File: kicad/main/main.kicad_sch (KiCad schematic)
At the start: 16 parts

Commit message: Progress on circuit design
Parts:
- removed D2, D3, D4: SS14, PCM_JLCPCB:D_SMA, symbol PCM_JLCPCB-Diodes:Schottky,SS14
- removed L2, L3, L4: 68uH, EasyEDA_Lib:IND-SMD_L6.0-W6.0_FNR60XXS, symbol EasyEDA_Lib:FNR6045S680MT
- removed R2, R3, R4: 150mΩ, Resistor_SMD:R_1206_3216Metric_Pad1.30x1.75mm_HandSolder, symbol Device:R
- removed U2, U3, U4: (no value), EasyEDA_Lib:SOT-89-5_L4.5-W2.5-P1.50-LS4.5-BR, symbol EasyEDA_Lib:CL6807
- added C1, C2: 10uF, PCM_JLCPCB:C_0805, symbol PCM_JLCPCB-Capacitors:0805,10uF
- added C10, C13: 1uF, PCM_JLCPCB:C_0402, symbol PCM_JLCPCB-Capacitors:0402,1uF
- added C11, C12, C14, C3, C4, C5, C6, C7, C8: 100nF, PCM_JLCPCB:C_0402, symbol PCM_JLCPCB-Capacitors:0402,100nF
- added J1, J4, J5: Conn_01x02, Connector_Wire:SolderWire-0.75sqmm_1x02_P4.8mm_D1.25mm_OD2.3mm, symbol Connector_Generic:Conn_01x02
- added J2, J3: Conn_01x03, symbol Connector_Generic:Conn_01x03
- added J6: Connector, USB-TYPE-C-16P, PCM_JLCPCB:TYPE-C-SMD_HX-TYPE-C-16PIN, symbol PCM_JLCPCB-Extended:Connector, USB-TYPE-C-16P
- added R2, R3: 5.1kΩ, PCM_JLCPCB:R_0402, symbol PCM_JLCPCB-Resistors:0402,5.1kΩ
- added R4, R5: 27Ω, PCM_JLCPCB:R_0603, symbol PCM_JLCPCB-Resistors:0603,27Ω
- added R6: 1kΩ, PCM_JLCPCB:R_0402, symbol PCM_JLCPCB-Resistors:0402,1kΩ
- added S1, S2: Tactile Button, 160gf, PCM_JLCPCB:SW_TS-1088-AR02016, symbol PCM_JLCPCB-Connectors_Buttons:Tactile Button, 160gf, 12V, 50mA, 4.0mm
- added U2: XC6206P332MR, PCM_JLCPCB:SOT-23-3_L2.9-W1.6-P1.90-LS2.8-BR, symbol PCM_JLCPCB-Power:LDO, 3.3V, 0.2A
- added U3: (no value), EasyEDA_Lib:SOIC-8_L5.3-W5.3-P1.27-LS8.0-BL, symbol EasyEDA_Lib:W25Q16JVSSIQTR
- added U5: RP2040, PCM_JLCPCB:QFN-56-1EP_7x7mm_P0.4mm_EP3.2x3.2mm_ThermalVias, symbol PCM_JLCPCB-Extended:MCU, RP2040
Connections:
- net GND: now also C1.2, C10.2, C11.2, C12.2, C13.2, C14.1, C2.2, C3.2, C4.2, C5.2, C6.2, C7.2, C8.2, J2.3 (Pin_3), J3.3 (Pin_3), J6.A12B1 (GND), J6.B12A1 (GND), J6.S1 (SHIELD), R2.2, R3.1, S1.2 (B), S2.2 (B), U2.1 (GND), U3.4 (GND), U5.57 (GND)
- net +12V renamed +5V
- net +5V: now also C1.1, J2.1 (Pin_1), J3.1 (Pin_1), J4.1 (Pin_1), J5.1 (Pin_1), J6.A9B4 (VBUS), J6.B9A4 (VBUS), U2.3 (VIN)
- net Red+ renamed LED+
- net LED+: now also J1.1 (Pin_1)
- net Red- renamed LED-
- net LED-: now also J1.2 (Pin_2)
- net Red_PWM renamed LED_PWM
- new net: J6.A5 (CC1), R2.1
- new net: J6.B5 (CC2), R3.2
- new net: R5.1, U5.46 (USB_DM)
- new net: R4.2, U5.47 (USB_DP)
- new net +1.1V: C10.1, C11.1, C12.1, U5.23 (DVDD), U5.45 (VREG_VOUT), U5.50 (DVDD)
- new net +3.3V: C13.1, C14.2, C2.1, C3.1, C4.1, C5.1, C6.1, C7.1, C8.1, U2.2 (VOUT), U3.8 (VCC), U5.1 (IOVDD), U5.10 (IOVDD), U5.22 (IOVDD), U5.33 (IOVDD), U5.42 (IOVDD), U5.43 (ADC_AVDD), U5.44 (VREG_IN), U5.48 (USB_VDD), U5.49 (IOVDD)
- new net Boot Button: R6.1, S1.1 (A)
- new net Data In: U5.3 (GPIO1)
- new net Pan: J2.2 (Pin_2), U5.4 (GPIO2)
- new net QSPI_SCLK: U3.6 (CLK)
- new net QSPI_SD0: U3.5 (DI/IO0)
- new net QSPI_SD1: U3.2 (DO/IO1)
- new net QSPI_SD2: U3.3 (IO2)
- new net QSPI_SD3: U3.7 (IO3)
- new net QSPI_SS: R6.2, U3.1 (/CS)
- new net Reset Button: S2.1 (A)
- new net T Board: J4.2 (Pin_2), U5.38 (GPIO26_ADC0)
- new net T LED: J5.2 (Pin_2), U5.39 (GPIO27_ADC1)
- new net Tilt: J3.2 (Pin_2), U5.5 (GPIO3)
- new net USB D+: J6.A6 (D+), J6.B6 (D+), R4.1
- new net USB D-: J6.A7 (D-), J6.B7 (D-), R5.2
- no-connect marks 0 -> 2
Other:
- moved on the sheet: D1, L1, R1, U1

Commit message: Schematic Progress
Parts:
- added C9: 10uF, PCM_JLCPCB:C_0805, symbol PCM_JLCPCB-Capacitors:0805,10uF
- added J7, J8: Conn_01x02, Connector_Wire:SolderWire-0.75sqmm_1x02_P4.8mm_D1.25mm_OD2.3mm, symbol Connector_Generic:Conn_01x02
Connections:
- net +5V: now also C9.1, J7.1 (Pin_1), J8.1 (Pin_1)
- net GND: now also C9.2, J7.2 (Pin_2), J8.2 (Pin_2)
- net Reset Button: now also U5.26 (RUN)

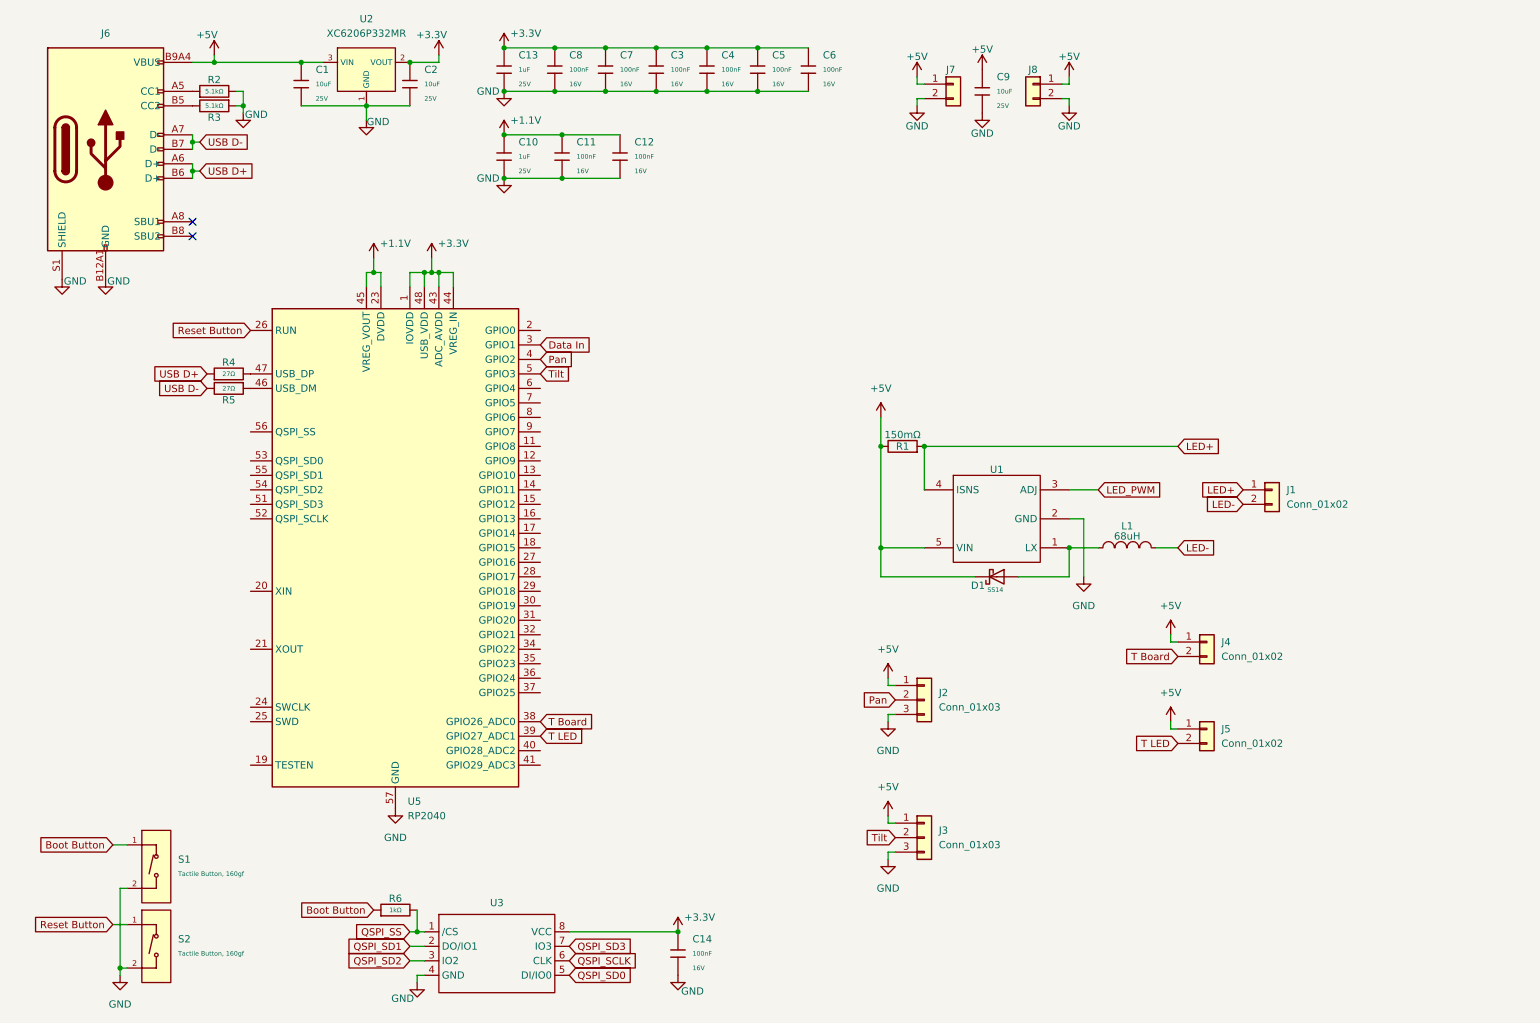
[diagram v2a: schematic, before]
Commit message: Schematic changes
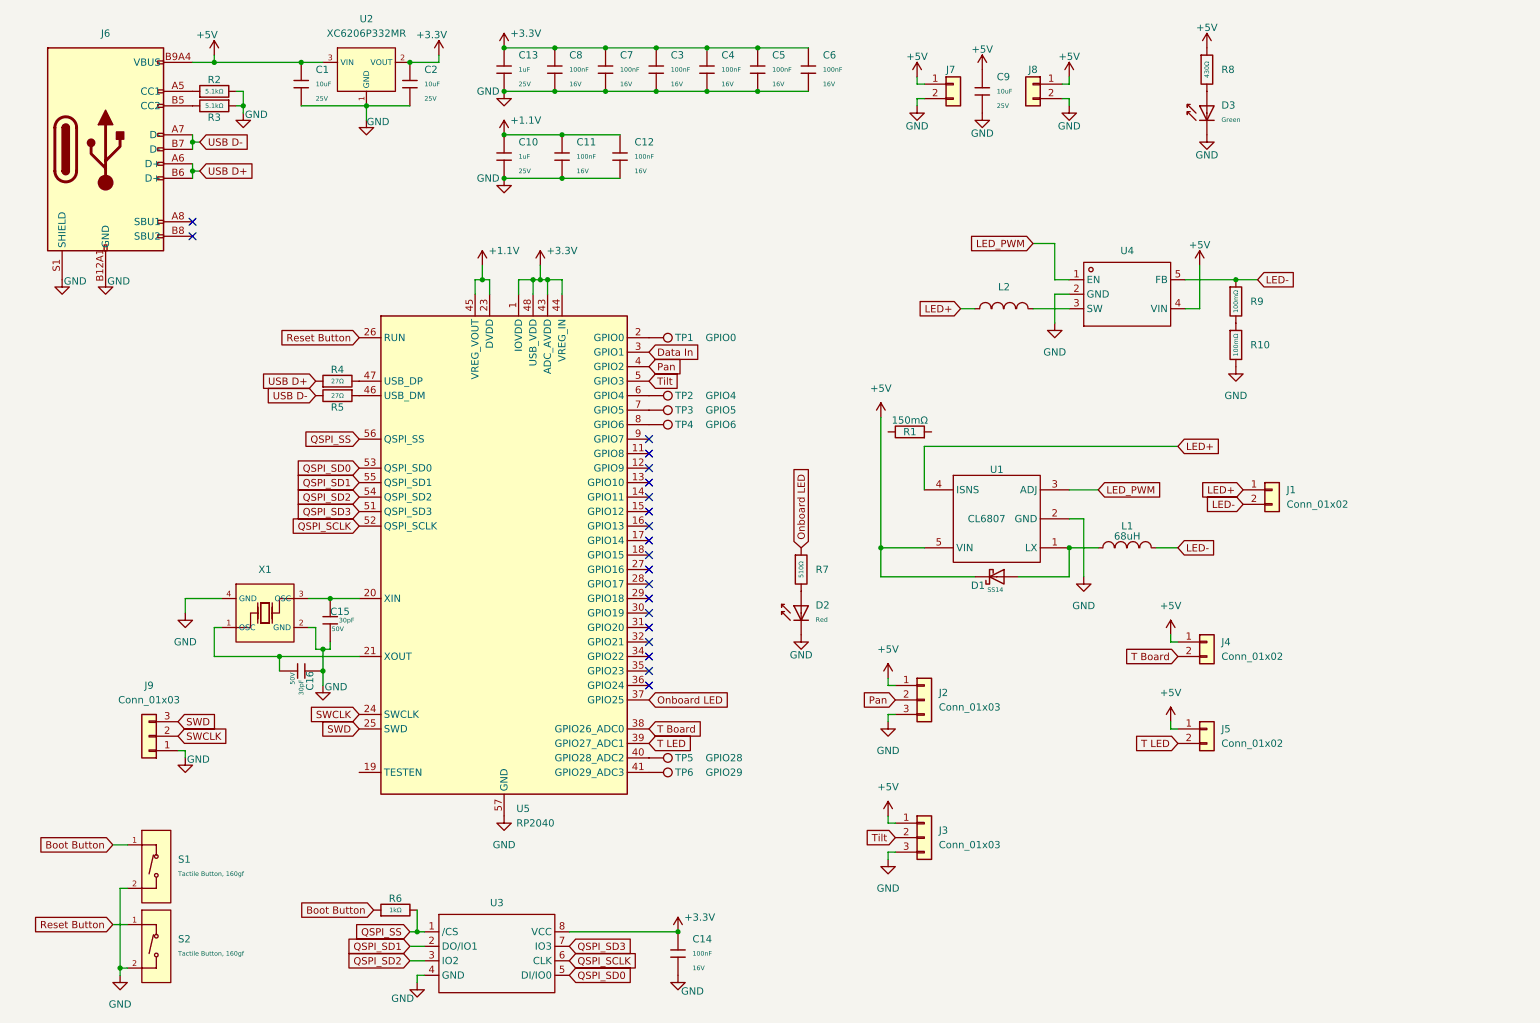
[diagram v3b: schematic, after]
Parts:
- added C15, C16: 30pF, PCM_JLCPCB:C_0402, symbol PCM_JLCPCB-Capacitors:0402,30pF
- added D2: Red, PCM_JLCPCB:D_0603, symbol PCM_JLCPCB-Diodes:LED,0603,Red
- added D3: Green, PCM_JLCPCB:D_0805, symbol PCM_JLCPCB-Diodes:LED,0805,Green
- added J9: Conn_01x03, symbol Connector_Generic:Conn_01x03
- added L2: 4.7uH, EasyEDA_Lib:IND-SMD_L3.5-W3.0, symbol EasyEDA_Lib:SM3521-4R7MT
- added R10, R9: 100mΩ, PCM_JLCPCB:R_1206, symbol PCM_JLCPCB-Resistors:1206,100mΩ
- added R7: 510Ω, PCM_JLCPCB:R_0402, symbol PCM_JLCPCB-Resistors:0402,510Ω
- added R8: 430Ω, PCM_JLCPCB:R_0603, symbol PCM_JLCPCB-Resistors:0603,430Ω
- added TP1: GPIO0, symbol Connector:TestPoint
- added TP2: GPIO4, symbol Connector:TestPoint
- added TP3: GPIO5, symbol Connector:TestPoint
- added TP4: GPIO6, symbol Connector:TestPoint
- added TP5: GPIO28, symbol Connector:TestPoint
- added TP6: GPIO29, symbol Connector:TestPoint
- added U4: (no value), EasyEDA_Lib:SOT-23-5_L3.0-W1.7-P0.95-LS2.8-BR, symbol EasyEDA_Lib:PAM2804AAB010
- added X1: X322512MSB4SI, PCM_JLCPCB:CRYSTAL-SMD_4P-L3.2-W2.5-BL, symbol PCM_JLCPCB-Crystals:Crystal, 12MHz, 20pF
- U1: value (none) -> CL6807
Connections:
- net +5V: now also R8.1, U4.4 (VIN); no longer R1.1
- net GND: now also C15.2, C16.1, D2.1, D3.1, J9.1 (Pin_1), R10.2, U4.2 (GND), X1.2 (GND), X1.4 (GND)
- net LED+: now also L2.1; no longer R1.2
- net LED-: now also R9.1, U4.5 (FB)
- net LED_PWM: now also U4.1 (EN)
- net QSPI_SCLK: now also U5.52 (QSPI_SCLK)
- net QSPI_SD0: now also U5.53 (QSPI_SD0)
- net QSPI_SD1: now also U5.55 (QSPI_SD1)
- net QSPI_SD2: now also U5.54 (QSPI_SD2)
- net QSPI_SD3: now also U5.51 (QSPI_SD3)
- net QSPI_SS: now also U5.56 (QSPI_SS)
- net at U5.2 (GPIO0): now also TP1.1
- net at U5.20 (XIN): now also C15.1, X1.3 (OSC)
- net at U5.21 (XOUT): now also C16.2, X1.1 (OSC)
- net SWCLK: now reaches U5.24 (SWCLK)
- net SWCLK: now also J9.2 (Pin_2)
- net SWD: now reaches U5.25 (SWD)
- net SWD: now also J9.3 (Pin_3)
- net Onboard LED: now reaches U5.37 (GPIO25)
- net Onboard LED: now also R7.1
- net at U5.40 (GPIO28_ADC2): now also TP5.1
- net at U5.41 (GPIO29_ADC3): now also TP6.1
- net at U5.6 (GPIO4): now also TP2.1
- net at U5.7 (GPIO5): now also TP3.1
- net at U5.8 (GPIO6): now also TP4.1
- new net: R10.1, R9.2
- new net: D3.2, R8.2
- new net: D2.2, R7.2
- new net: L2.2, U4.3 (SW)
- no-connect marks 2 -> 20
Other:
- moved on the sheet: R4, R5, U5

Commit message: First draft of schematic complete
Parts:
- J1, J7, J8: footprint Connector_Wire:SolderWire-0.75sqmm_1x02_P4.8mm_D1.25mm_OD2.3mm -> solder-pads:2-position
- J2, J3: footprint (none) -> solder-pads:3-position
- J4, J5: footprint Connector_Wire:SolderWire-0.75sqmm_1x02_P4.8mm_D1.25mm_OD2.3mm -> Connector_PinHeader_2.54mm:PinHeader_1x02_P2.54mm_Vertical
- J9: footprint (none) -> Connector_PinHeader_2.54mm:PinHeader_1x03_P2.54mm_Vertical
- TP1, TP2, TP3, TP4, TP5, TP6: footprint (none) -> TestPoint:TestPoint_Pad_D1.0mm
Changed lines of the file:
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@@
 			)
 		)
-		(property "Footprint" "Connector_Wire:SolderWire-0.75sqmm_1x02_P4.8mm_D1.25mm_OD2.3mm"
+		(property "Footprint" "Connector_PinHeader_2.54mm:PinHeader_1x02_P2.54mm_Vertical"
 			(at 219.71 124.46 0)
 			(hide yes)
@@
 			)
 		)
-		(property "Footprint" ""
+		(property "Footprint" "TestPoint:TestPoint_Pad_D1.0mm"
 			(at 121.92 91.44 0)
 			(hide yes)
@@
 			)
 		)
-		(property "Footprint" ""
+		(property "Footprint" "TestPoint:TestPoint_Pad_D1.0mm"
 			(at 121.92 152.4 0)
 			(hide yes)
@@
 			)
 		)
-		(property "Footprint" "Connector_Wire:SolderWire-0.75sqmm_1x02_P4.8mm_D1.25mm_OD2.3mm"
+		(property "Footprint" "solder-pads:2-position"
 			(at 175.26 26.67 0)
 			(hide yes)
@@
 			)
 		)
-		(property "Footprint" ""
+		(property "Footprint" "solder-pads:3-position"
 			(at 170.18 134.62 0)
 			(hide yes)
@@
 			)
 		)
-		(property "Footprint" ""
+		(property "Footprint" "TestPoint:TestPoint_Pad_D1.0mm"
 			(at 121.92 86.36 0)
 			(hide yes)
@@
 			)
 		)
-		(property "Footprint" ""
+		(property "Footprint" "TestPoint:TestPoint_Pad_D1.0mm"
 			(at 121.92 88.9 0)
 			(hide yes)
@@
 			)
 		)
-		(property "Footprint" ""
+		(property "Footprint" "TestPoint:TestPoint_Pad_D1.0mm"
 			(at 121.92 149.86 0)
 			(hide yes)
@@
 			)
 		)
-		(property "Footprint" "Connector_Wire:SolderWire-0.75sqmm_1x02_P4.8mm_D1.25mm_OD2.3mm"
+		(property "Footprint" "solder-pads:2-position"
 			(at 231.14 97.79 0)
 			(hide yes)
@@
 			)
 		)
-		(property "Footprint" ""
+		(property "Footprint" "Connector_PinHeader_2.54mm:PinHeader_1x03_P2.54mm_Vertical"
 			(at 34.29 140.97 0)
 			(hide yes)
@@
 			)
 		)
-		(property "Footprint" ""
+		(property "Footprint" "TestPoint:TestPoint_Pad_D1.0mm"
 			(at 121.92 76.2 0)
 			(hide yes)
@@
 			)
 		)
-		(property "Footprint" "Connector_Wire:SolderWire-0.75sqmm_1x02_P4.8mm_D1.25mm_OD2.3mm"
+		(property "Footprint" "solder-pads:2-position"
 			(at 189.23 26.67 0)
 			(hide yes)
@@
 			)
 		)
-		(property "Footprint" "Connector_Wire:SolderWire-0.75sqmm_1x02_P4.8mm_D1.25mm_OD2.3mm"
+		(property "Footprint" "Connector_PinHeader_2.54mm:PinHeader_1x02_P2.54mm_Vertical"
 			(at 219.71 139.7 0)
 			(hide yes)
@@
 			)
 		)
-		(property "Footprint" ""
+		(property "Footprint" "solder-pads:3-position"
 			(at 170.18 158.75 0)
 			(hide yes)

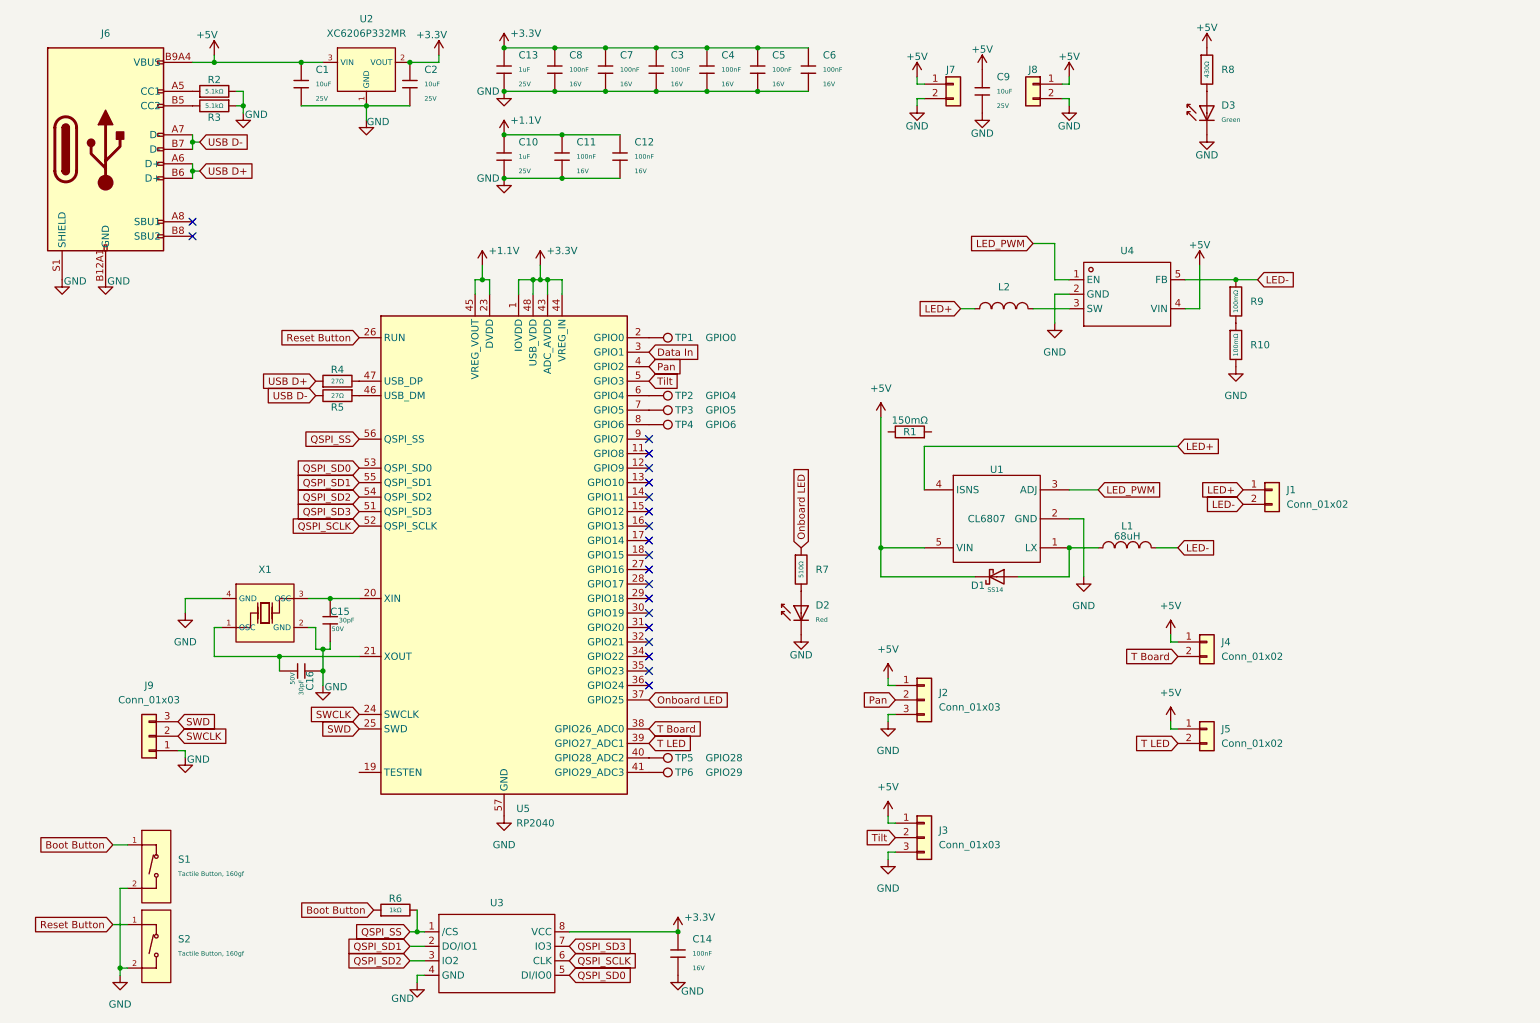
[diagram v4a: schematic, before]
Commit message: Removed SWD connections and added "DMX" connection
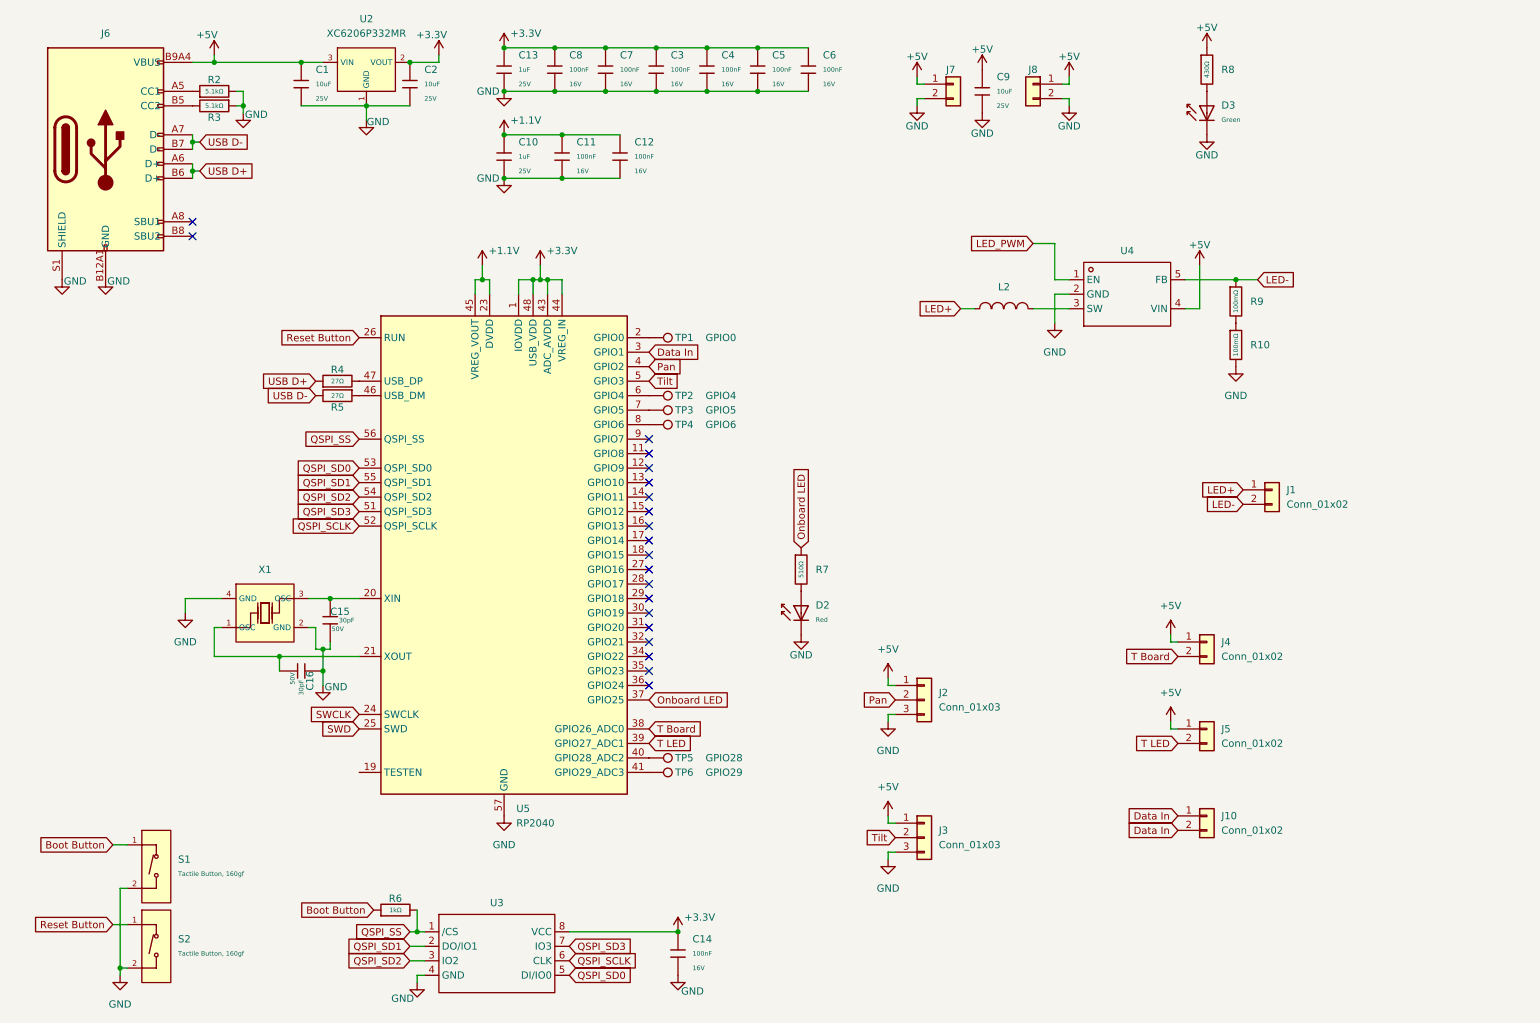
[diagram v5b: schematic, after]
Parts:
- removed D1: SS14, PCM_JLCPCB:D_SMA, symbol PCM_JLCPCB-Diodes:Schottky,SS14
- removed J9: Conn_01x03, Connector_PinHeader_2.54mm:PinHeader_1x03_P2.54mm_Vertical, symbol Connector_Generic:Conn_01x03
- removed L1: 68uH, EasyEDA_Lib:IND-SMD_L6.0-W6.0_FNR60XXS, symbol EasyEDA_Lib:FNR6045S680MT
- removed R1: 150mΩ, Resistor_SMD:R_1206_3216Metric_Pad1.30x1.75mm_HandSolder, symbol Device:R
- removed U1: CL6807, EasyEDA_Lib:SOT-89-5_L4.5-W2.5-P1.50-LS4.5-BR, symbol EasyEDA_Lib:CL6807
- added J10: Conn_01x02, solder-pads:2-position, symbol Connector_Generic:Conn_01x02
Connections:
- net Data In: now also J10.1 (Pin_1), J10.2 (Pin_2)
